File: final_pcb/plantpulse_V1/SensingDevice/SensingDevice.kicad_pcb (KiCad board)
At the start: 2 copper layers, 60.2 x 37.4 mm, 7 parts, among them J1 SEN0193, J2 LiPo Battery, U2 SHT31-DIS-B2.5KS

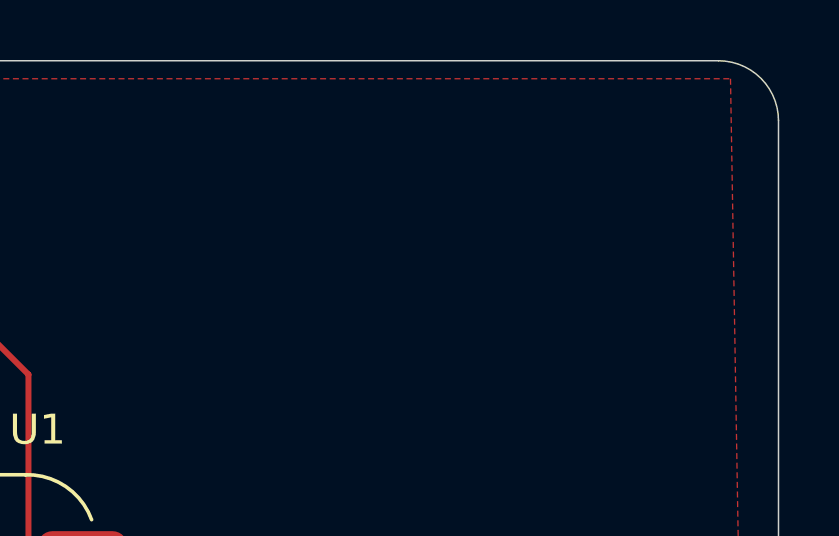
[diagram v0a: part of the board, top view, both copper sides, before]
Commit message: src code for sensing device update
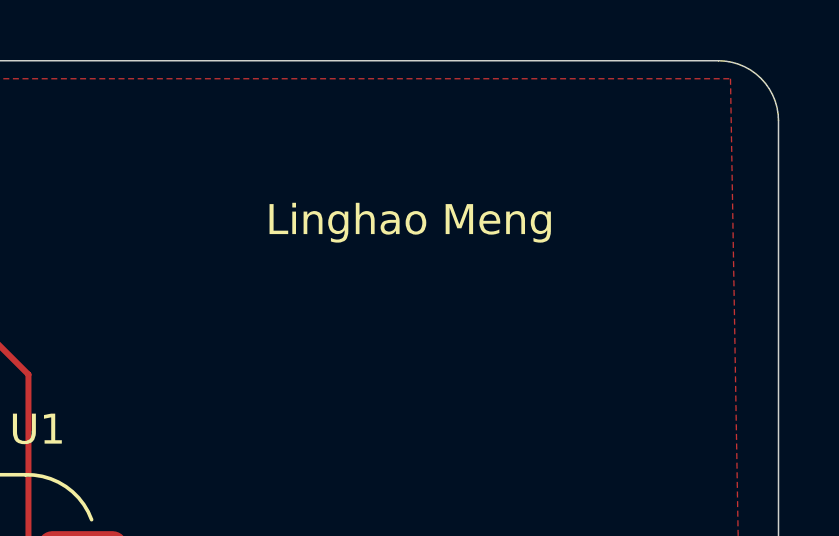
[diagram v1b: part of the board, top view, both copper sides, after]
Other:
- board text added: "Linghao Meng"
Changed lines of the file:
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@@
+		)
+	)
+	(gr_text "Linghao Meng"
+		(at 148.5 74.5 0)
+		(layer "F.SilkS")
+		(effects
+			(font
+				(size 1 1)
+				(thickness 0.1)
+			)
+			(justify left bottom)
 		)
 	)
